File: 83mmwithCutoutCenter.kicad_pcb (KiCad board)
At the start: 2 copper layers, 83 x 55 mm, 41 parts, among them J1 Conn_01x08, U1 ., Y1 ABM8

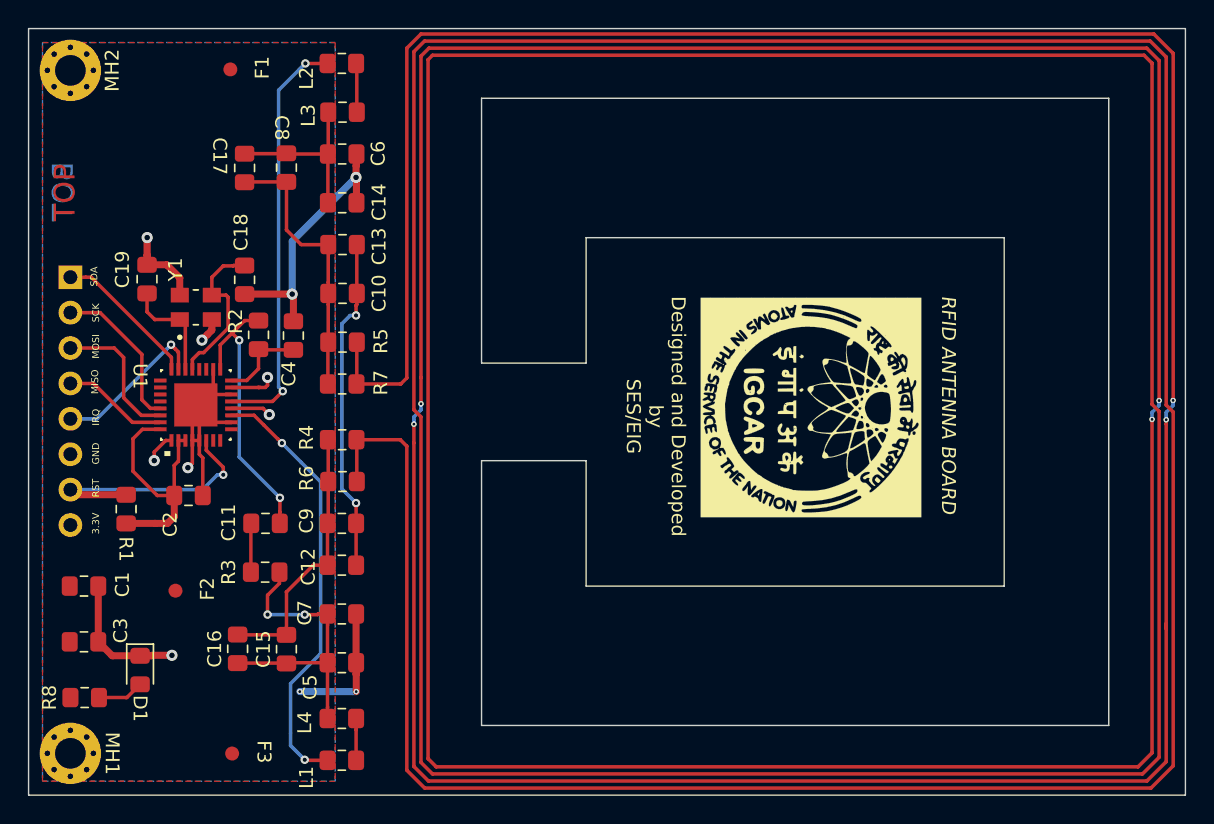
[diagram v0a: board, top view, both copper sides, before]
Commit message: Centre Cutout
Added gerber and layout files for center cutout
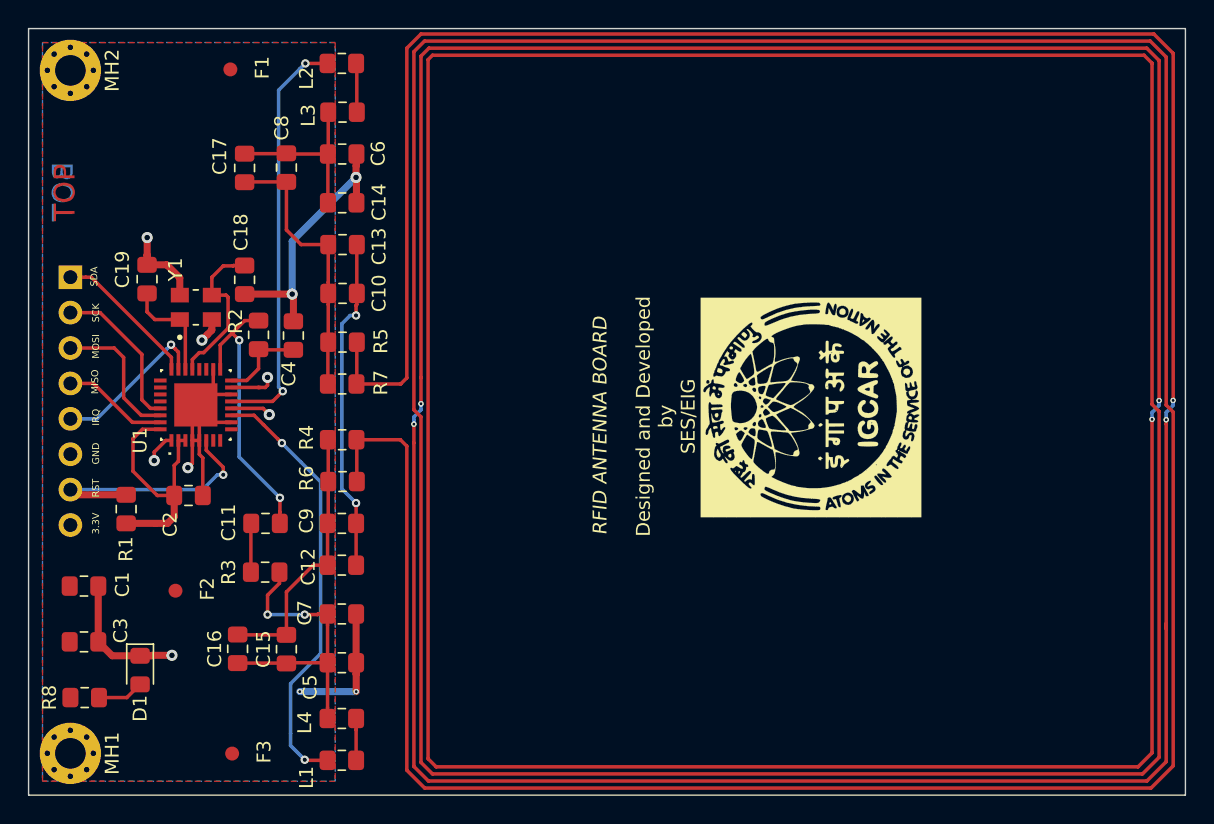
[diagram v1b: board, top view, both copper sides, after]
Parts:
- turned G*** to 90 degrees
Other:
- outline, holes or cut-outs redrawn
